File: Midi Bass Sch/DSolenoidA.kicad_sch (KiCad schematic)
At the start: 120 parts

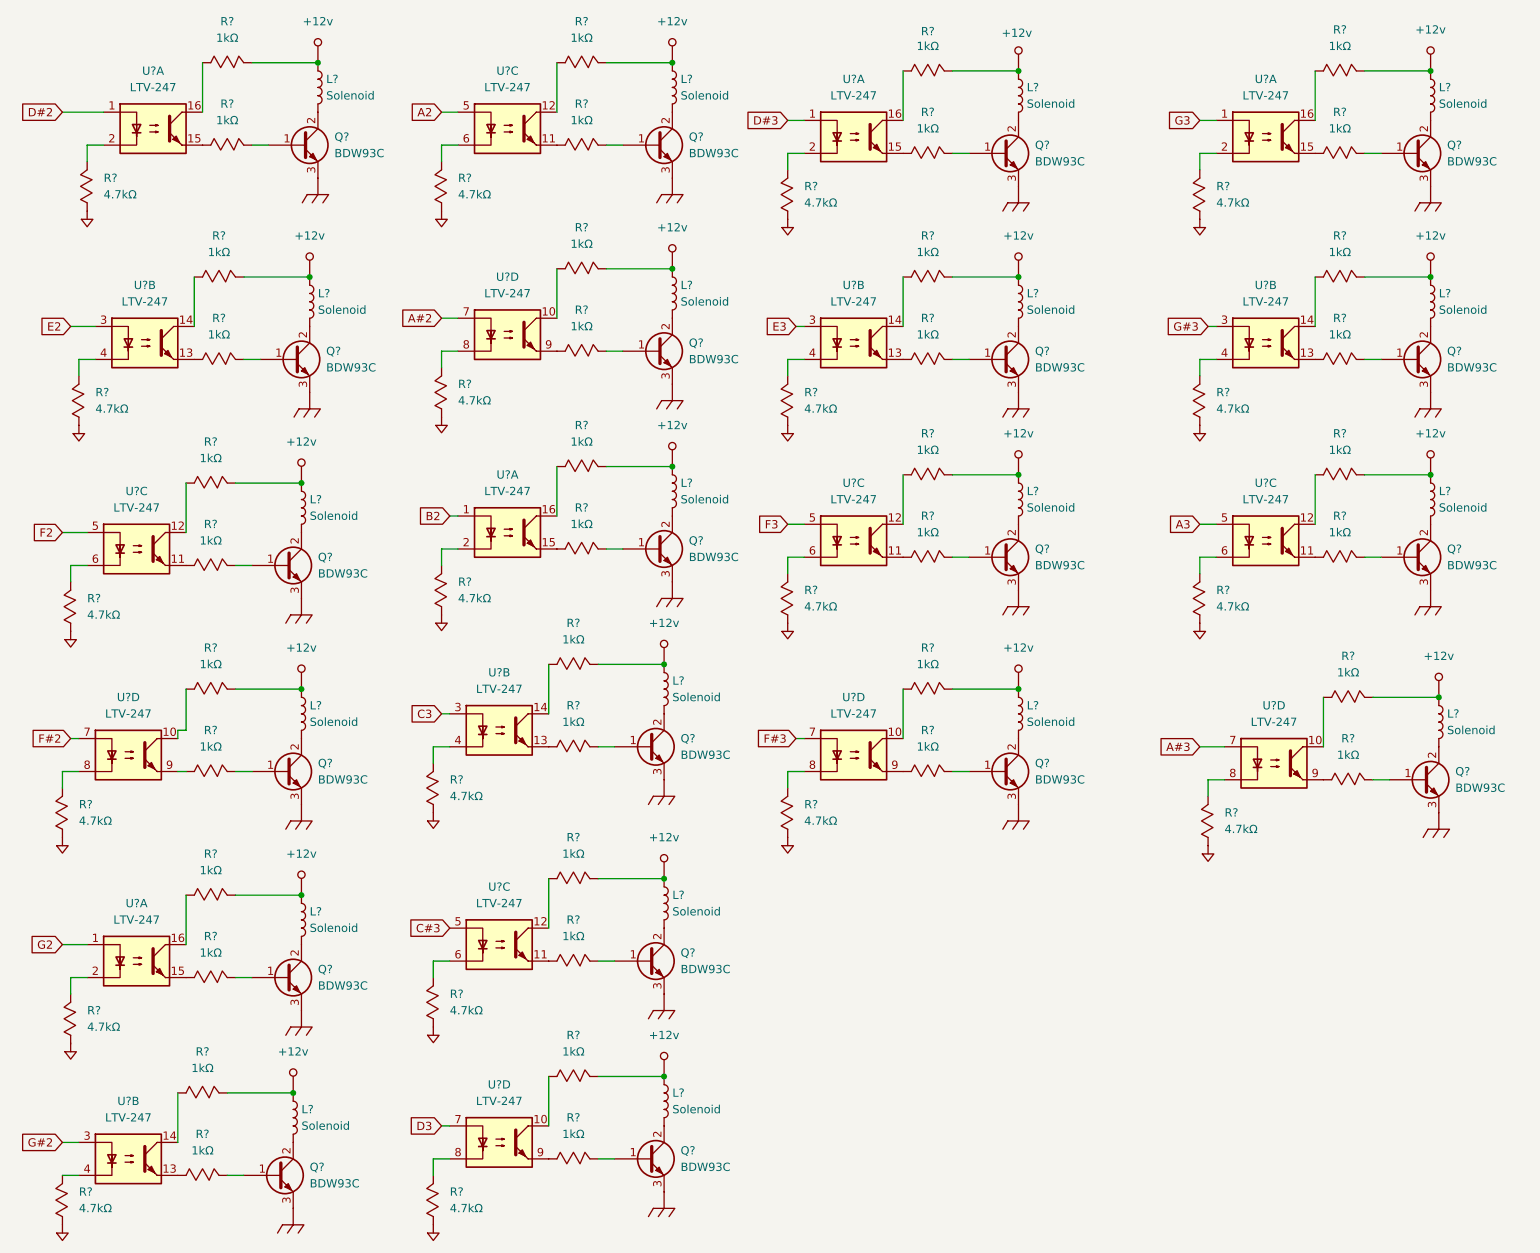
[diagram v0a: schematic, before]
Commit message: added solenoid array for the G slave
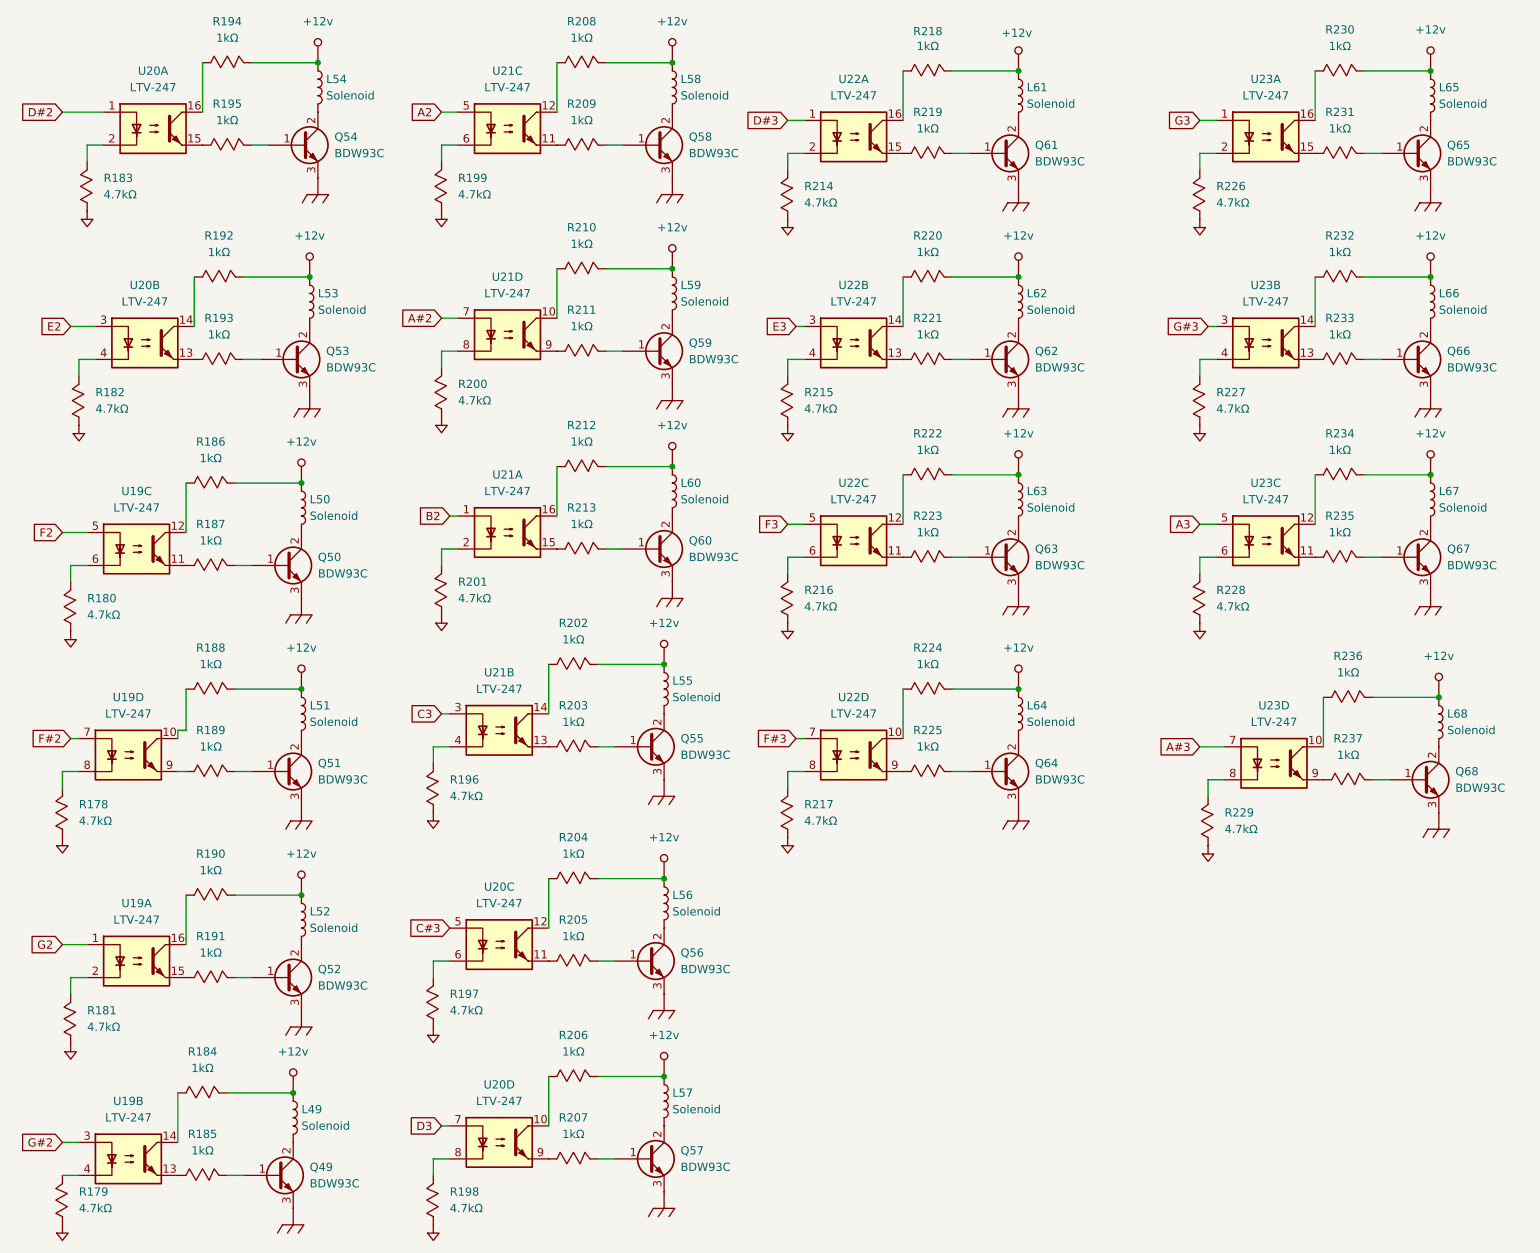
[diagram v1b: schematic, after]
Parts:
- gave numbers to parts that had none: 105

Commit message: added footprints to kicad schematic still need footprint for din connector
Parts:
- Q49, Q50, Q51, Q52, Q53, Q54, Q55, Q56, Q57, Q58, Q59, Q60, Q61, Q62, Q63, Q64, Q65, Q66, Q67, Q68: footprint (none) -> Package_TO_SOT_THT:TO-220-3_Vertical
- R178, R179, R180, R181, R182, R183, R184, R185, R186, R187, R188, R189, R190, R191, R192, R193, R194, R195, R196, R197, R198, R199, R200, R201, R202, R203, R204, R205, R206, R207, R208, R209, R210, R211, R212, R213, R214, R215, R216, R217, R218, R219, R220, R221, R222, R223, R224, R225, R226, R227, R228, R229, R230, R231, R232, R233, R234, R235, R236, R237: footprint (none) -> Resistor_SMD:R_0805_2012Metric_Pad1.20x1.40mm_HandSolder

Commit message: working on troubleshooting section of report
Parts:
- renumbered L49 to L53, L50 to L54, L51 to L55, L52 to L56, L53 to L57, L54 to L58, L55 to L59, L56 to L60, L57 to L61, L58 to L62, L59 to L63, L60 to L64, L61 to L65, L62 to L66, L63 to L67, L64 to L68, L65 to L69, L66 to L70, L67 to L71, L68 to L72, Q49 to Q53, Q50 to Q54, Q51 to Q55, Q52 to Q56, Q53 to Q57, Q54 to Q58, Q55 to Q59, Q56 to Q60, Q57 to Q61, Q58 to Q62, Q59 to Q63, Q60 to Q64, Q61 to Q65, Q62 to Q66, Q63 to Q67, Q64 to Q68, Q65 to Q69, Q66 to Q70, Q67 to Q71, Q68 to Q72, R178 to R190, R179 to R191, R180 to R192, R181 to R193, R182 to R194, R183 to R195, R184 to R196, R185 to R197, R186 to R198, R187 to R199, R188 to R200, R189 to R201, R190 to R202, R191 to R203, R192 to R204, R193 to R205, R194 to R206, R195 to R207, R196 to R208, R197 to R209, R198 to R210, R199 to R211, R200 to R212, R201 to R213, R202 to R214, R203 to R215, R204 to R216, R205 to R217, R206 to R218, R207 to R219, R208 to R220, R209 to R221, R210 to R222, R211 to R223, R212 to R224, R213 to R225, R214 to R226, R215 to R227, R216 to R228, R217 to R229, R218 to R230, R219 to R231, R220 to R232, R221 to R233, R222 to R234, R223 to R235, R224 to R236, R225 to R237, R226 to R238, R227 to R239, R228 to R240, R229 to R241, R230 to R242, R231 to R243, R232 to R244, R233 to R245, R234 to R246, R235 to R247, R236 to R248, R237 to R249, U19 to U21, U20 to U22, U21 to U23, U22 to U24, U23 to U25

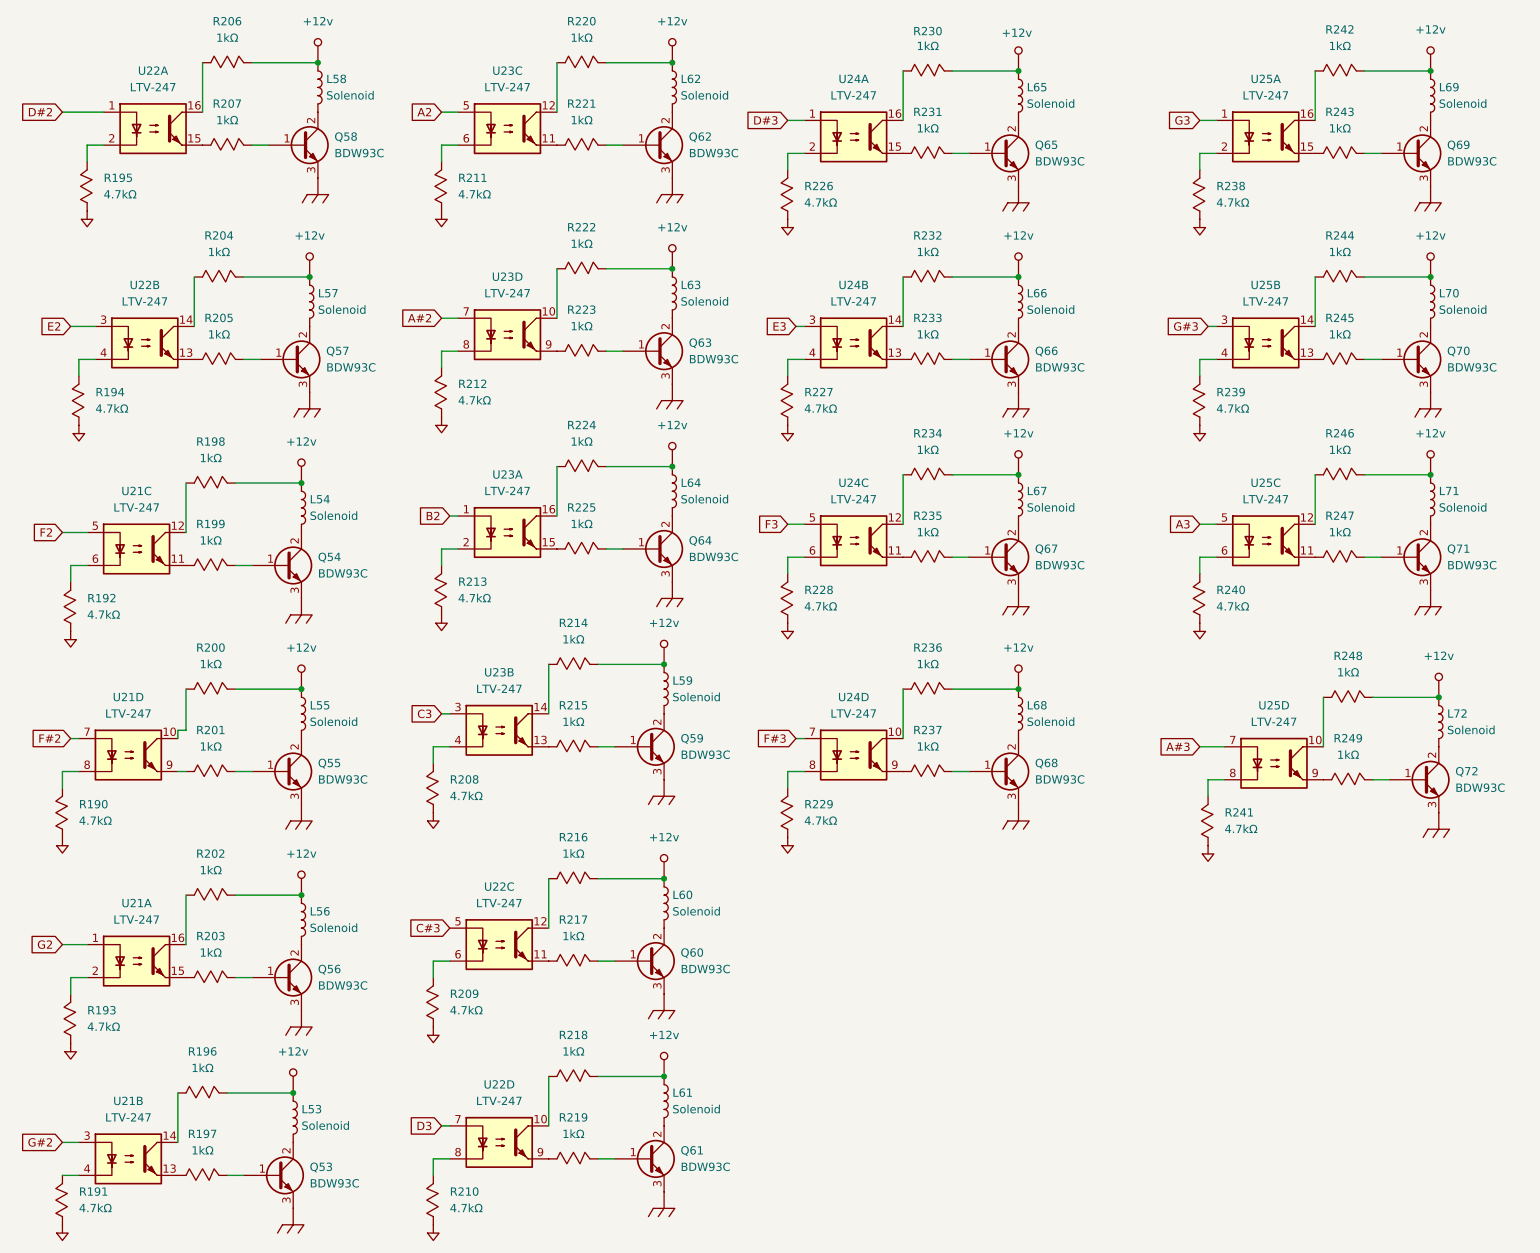
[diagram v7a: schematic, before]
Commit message: changed transistor for schematic
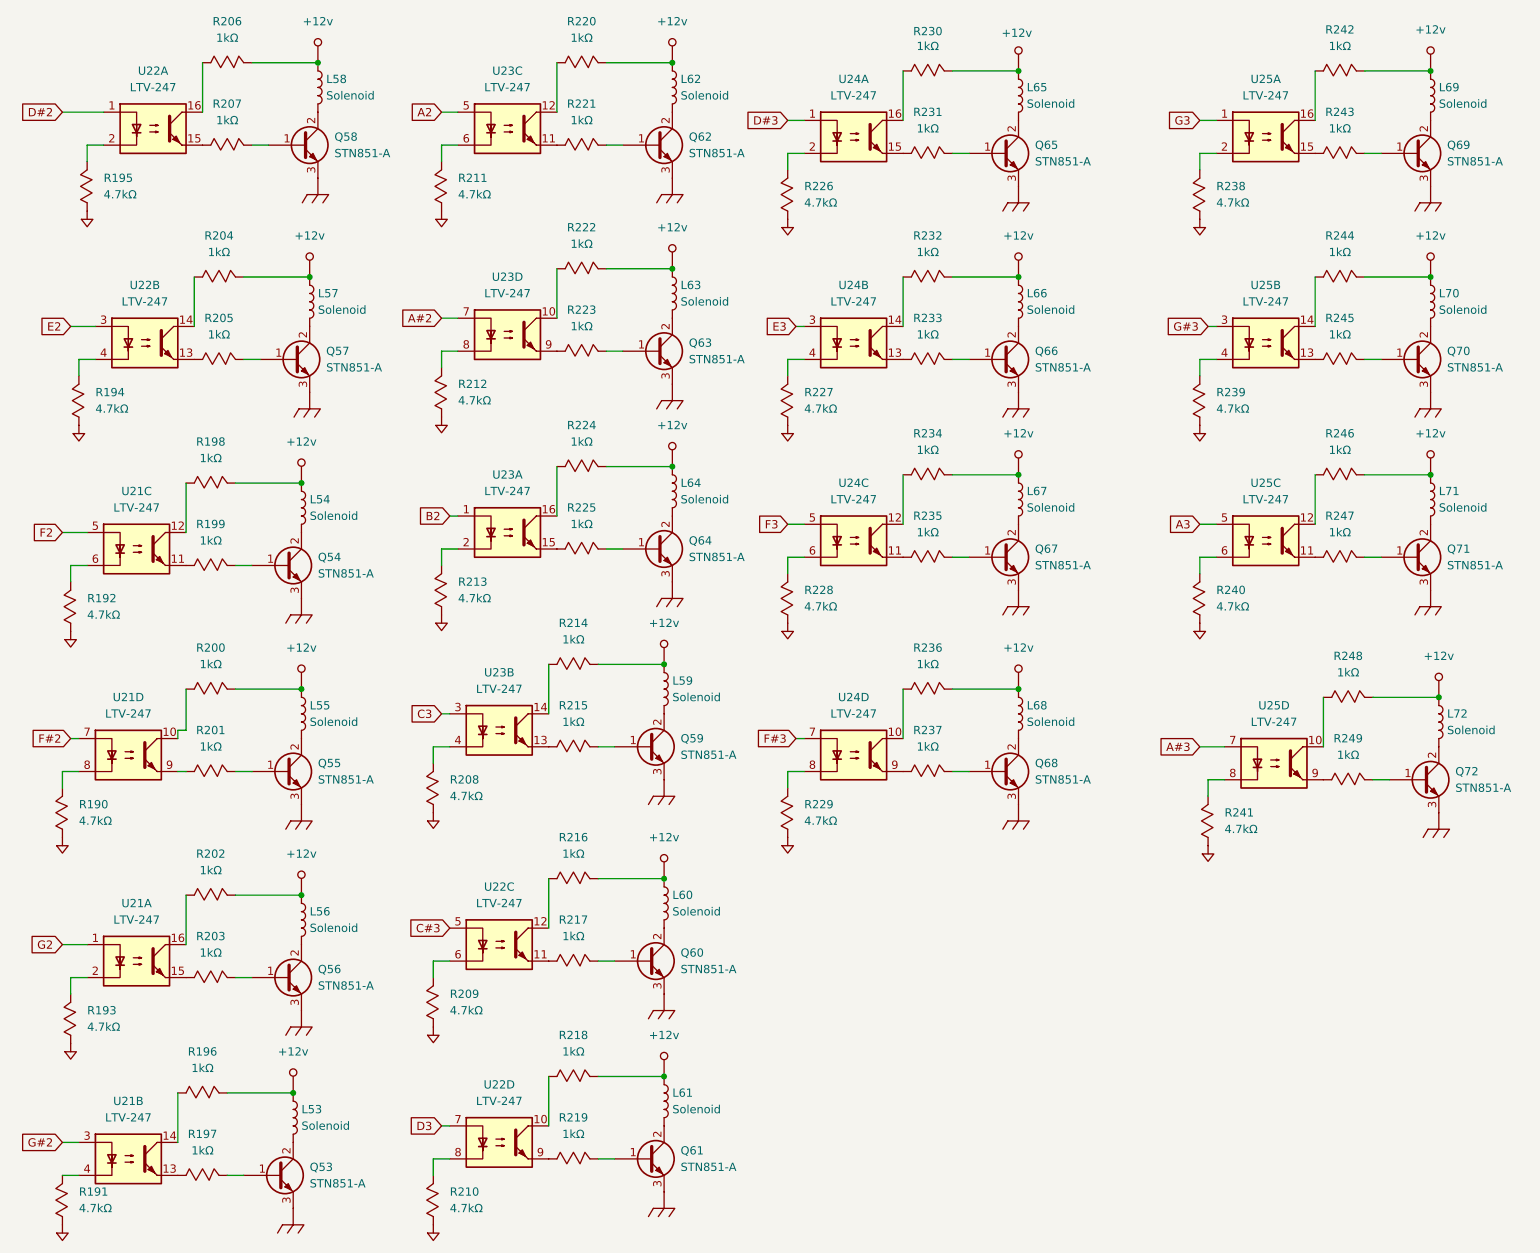
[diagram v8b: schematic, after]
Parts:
- Q53, Q54, Q55, Q56, Q57, Q58, Q59, Q60, Q61, Q62, Q63, Q64, Q65, Q66, Q67, Q68, Q69, Q70, Q71, Q72: value BDW93C -> STN851-A
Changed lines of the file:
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@@
 			)
 		)
-		(property "Value" "BDW93C"
+		(property "Value" "STN851-A"
 			(at 240.03 38.0999 0)
 			(effects
@@
 			)
 		)
-		(property "Value" "BDW93C"
+		(property "Value" "STN851-A"
 			(at 176.53 38.0999 0)
 			(effects
@@
 			)
 		)
-		(property "Value" "BDW93C"
+		(property "Value" "STN851-A"
 			(at 66.04 165.0999 0)
 			(effects
@@
 			)
 		)
-		(property "Value" "BDW93C"
+		(property "Value" "STN851-A"
 			(at 121.92 162.5599 0)
 			(effects
@@
 			)
 		)
-		(property "Value" "BDW93C"
+		(property "Value" "STN851-A"
 			(at 67.31 69.8499 0)
 			(effects
@@
 			)
 		)
-		(property "Value" "BDW93C"
+		(property "Value" "STN851-A"
 			(at 68.58 36.8299 0)
 			(effects
@@
 			)
 		)
-		(property "Value" "BDW93C"
+		(property "Value" "STN851-A"
 			(at 123.19 99.0599 0)
 			(effects
@@
 			)
 		)
-		(property "Value" "BDW93C"
+		(property "Value" "STN851-A"
 			(at 176.53 69.8499 0)
 			(effects
@@
 			)
 		)
-		(property "Value" "BDW93C"
+		(property "Value" "STN851-A"
 			(at 240.03 100.3299 0)
 			(effects
@@
 			)
 		)
-		(property "Value" "BDW93C"
+		(property "Value" "STN851-A"
 			(at 121.92 193.0399 0)
 			(effects
@@
 			)
 		)
-		(property "Value" "BDW93C"
+		(property "Value" "STN851-A"
 			(at 176.53 100.3299 0)
 			(effects
@@
 			)
 		)
-		(property "Value" "BDW93C"
+		(property "Value" "STN851-A"
 			(at 66.04 133.3499 0)
 			(effects
@@
 			)
 		)
-		(property "Value" "BDW93C"
+		(property "Value" "STN851-A"
 			(at 66.04 101.5999 0)
 			(effects
@@
 			)
 		)
-		(property "Value" "BDW93C"
+		(property "Value" "STN851-A"
 			(at 123.19 36.8299 0)
 			(effects
@@
 			)
 		)
-		(property "Value" "BDW93C"
+		(property "Value" "STN851-A"
 			(at 121.92 129.5399 0)
 			(effects
@@
 			)
 		)
-		(property "Value" "BDW93C"
+		(property "Value" "STN851-A"
 			(at 123.19 68.5799 0)
 			(effects
@@
 			)
 		)
-		(property "Value" "BDW93C"
+		(property "Value" "STN851-A"
 			(at 64.77 195.5799 0)
 			(effects
@@
 			)
 		)
-		(property "Value" "BDW93C"
+		(property "Value" "STN851-A"
 			(at 241.3 134.6199 0)
 			(effects
@@
 			)
 		)
-		(property "Value" "BDW93C"
+		(property "Value" "STN851-A"
 			(at 176.53 133.3499 0)
 			(effects
@@
 			)
 		)
-		(property "Value" "BDW93C"
+		(property "Value" "STN851-A"
 			(at 240.03 69.8499 0)
 			(effects
